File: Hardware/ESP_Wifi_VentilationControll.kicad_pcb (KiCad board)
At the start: 2 copper layers, 52 x 37 mm, 38 parts, among them J1 programming, Q1 2N3904, Q2 2N3904, SW1 RST, SW2 BOOT, U1 LM1117-3.3, U2 ESP-12E, U3 ILD207T_D207, U4 ILD207T_D207, U5 XD-45_MH_MINI

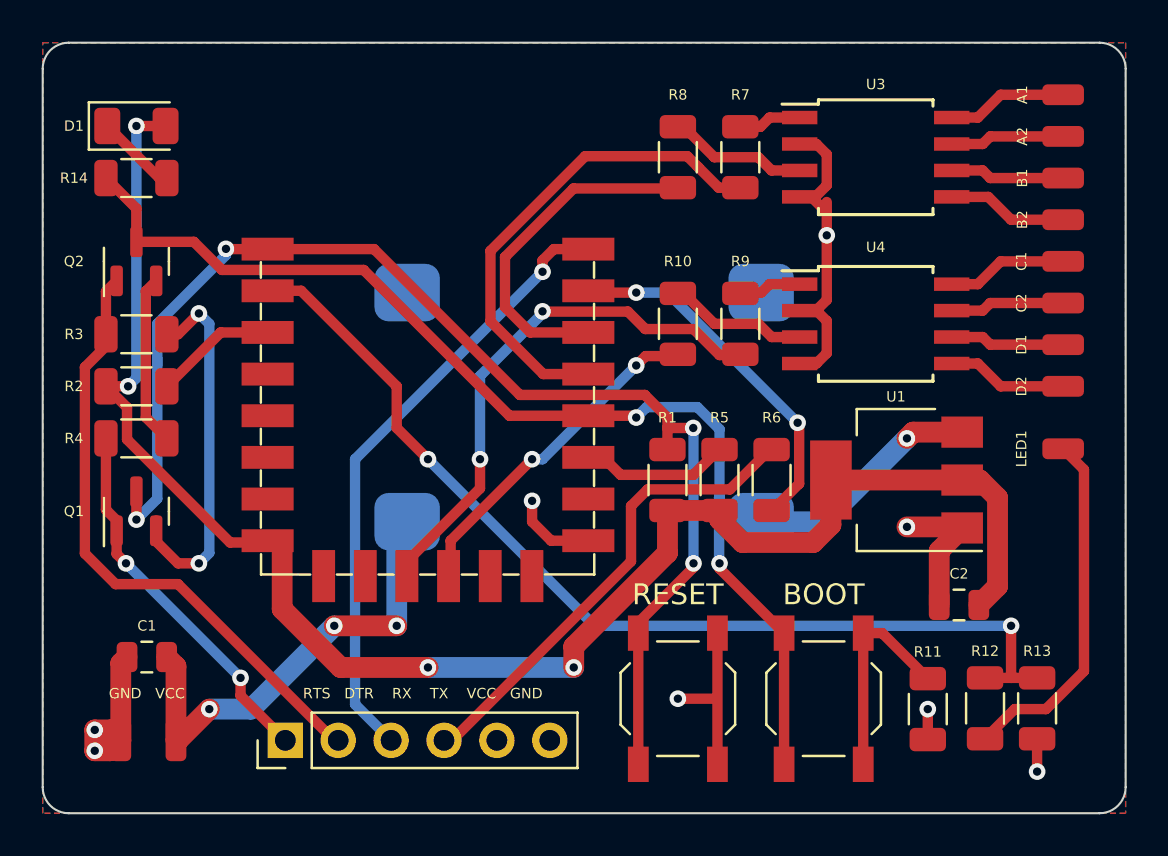
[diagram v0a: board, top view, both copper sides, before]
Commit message: fixed some footprints and added missing resistor
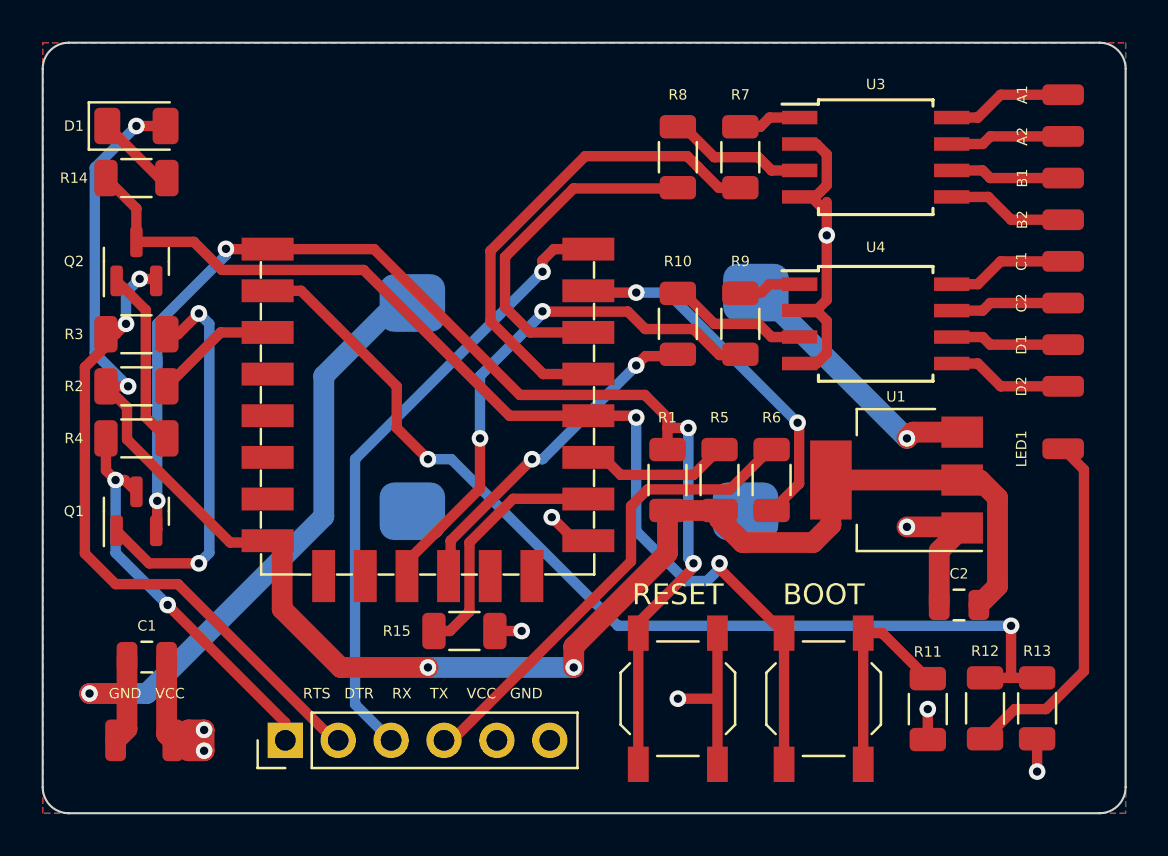
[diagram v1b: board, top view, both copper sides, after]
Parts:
- added R15: 4k7, Resistor_SMD:R_1206_3216Metric, F.Cu at (145.2, 107.8)
- Q1, Q2: value 2N3904 -> MMBT3904
- R11: value R -> 470
- moved TP11 2.90 mm to (128.5, 113.0)
- moved TP12 2.50 mm to (131.2, 113.0)
- moved U5 0.25 mm to (150.8, 97.0)
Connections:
- C1 pad 1: Net-(C1-Pad1) -> GND
- C1 pad 2: GND -> Net-(C1-Pad2)
- Q1 pad 1: /RTS -> Net-(Q1-Pad1)
- Q1 pad 3: Net-(Q1-Pad3) -> /RTS
- Q2 pad 1: /DTR -> Net-(Q2-Pad1)
- Q2 pad 2: Net-(Q2-Pad2) -> /DTR
- R1 pad 2: Net-(Q1-Pad3) -> Net-(Q1-Pad2)
- R3 pad 2: Net-(Q1-Pad2) -> Net-(Q1-Pad1)
- R4 pad 2: Net-(Q2-Pad2) -> Net-(Q2-Pad1)
- SW1 pad 2: Net-(Q1-Pad3) -> Net-(Q1-Pad2)
- TP11 pad 1: Net-(C1-Pad1) -> Net-(C1-Pad2)
- U2 pad 1: Net-(Q1-Pad3) -> Net-(Q1-Pad2)
- U2 pad 10: unconnected-(U2-Pad10) -> Net-(R15-Pad1)
- U5 pad 1: Net-(C1-Pad1) -> GND
- U5 pad 2: GND -> Net-(C1-Pad2)
- U5 pad 3: VCC -> GND
- U5 pad 4: GND -> VCC
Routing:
- net Net-(Q1-Pad3): track 61.0 -> 0.00 mm, vias 4 -> 0
- net Net-(Q1-Pad2): track 17.9 -> 59.7 mm, vias 2 -> 4
- net Net-(C1-Pad2): track 0.00 -> 33.3 mm, vias 0 -> 1
- net Net-(C1-Pad1): track 22.3 -> 0.00 mm, vias 3 -> 0
- net Net-(Q1-Pad1): track 0.00 -> 19.0 mm, vias 0 -> 2
- net Net-(R15-Pad1): track 0.00 -> 11.3 mm
- net Net-(Q2-Pad1): track 0.00 -> 8.56 mm
- net Net-(Q2-Pad2): track 8.19 -> 0.00 mm
- net +3V3: track 80.5 -> 81.8 mm
- net VCC: track 11.4 -> 12.7 mm
- net /RTS: track 18.1 -> 19.3 mm
- net /DTR: track 29.6 -> 30.7 mm, vias 0 -> 2
- net GND: track 44.6 -> 44.1 mm, vias 8 -> 9

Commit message: rendered new pictures
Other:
- board text added: "Wifi ventilation controll V2.0 designed by: stefarn"
- board text removed: "Wifi ventilation controll V1.0 designed by: stefarn"
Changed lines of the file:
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@@
   (gr_arc (start 126.25 116.5) (mid 125.366117 116.133883) (end 125 115.25) (layer "Edge.Cuts") (width 0.1))
   (gr_line (start 177 80.75) (end 177 115.25) (layer "Edge.Cuts") (width 0.1))
-  (gr_text "Wifi ventilation controll V1.0\ndesigned by: stefarn" (at 151 84) (layer "B.SilkS")
+  (gr_text "Wifi ventilation controll V2.0\ndesigned by: stefarn" (at 151 84) (layer "B.SilkS")
     (effects (font (size 1 1) (thickness 0.125)) (justify mirror))
   )

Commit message: e
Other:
- board text added: "RTS DTR TX RX VCC GND"
- board text removed: "RTS DTR RX TX VCC GND"
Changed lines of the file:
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@@
     (property "Sheetname" "")
     (attr smd)
-    (fp_text reference "U5" (at 0 9.75 180 unlocked) (layer "B.SilkS")
+    (fp_text reference "U5" (at 0 9.75 180 unlocked) (layer "B.Fab")
       (effects (font (size 1 1) (thickness 0.15)) (justify mirror))
     )
@@
     (effects (font (size 1 1) (thickness 0.25)))
   )
-  (gr_text "RTS   DTR    RX    TX    VCC   GND " (at 143.25 110.75) (layer "F.SilkS")
+  (gr_text "RTS   DTR    TX    RX    VCC   GND " (at 143.25 110.75) (layer "F.SilkS")
     (effects (font (size 0.5 0.5) (thickness 0.125)))
   )
